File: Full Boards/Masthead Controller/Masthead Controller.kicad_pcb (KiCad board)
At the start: 4 copper layers, 80 x 150.1 mm, 177 parts, among them Q1 2N7002, Q2 2N7002, Q3 BSS138P,215, Q4 BSS138P,215, SW1 SW_MEC_5G, SW2 SW_MEC_5G

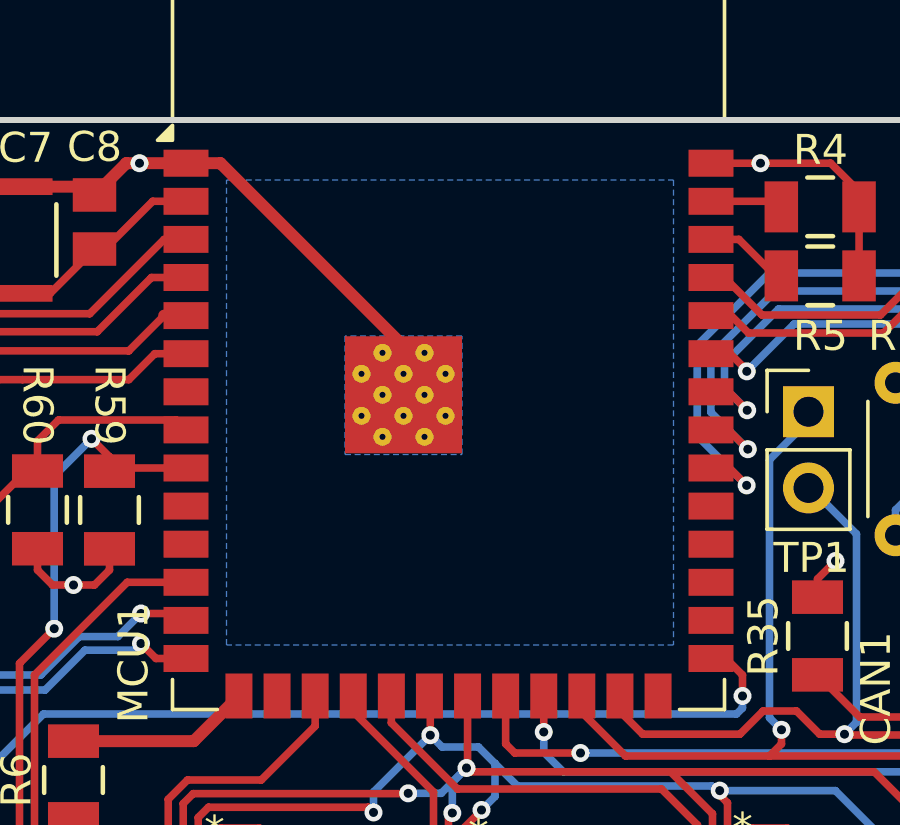
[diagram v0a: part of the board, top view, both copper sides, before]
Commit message: Clones the ESP32-S3-WROOM-1 footprint to bump the vias to 0.3mm. Added a stitched ground under the ESP32 MCU to help further with cooling.
Signed-off-by: digimer <digital.mermaid@gmail.com>
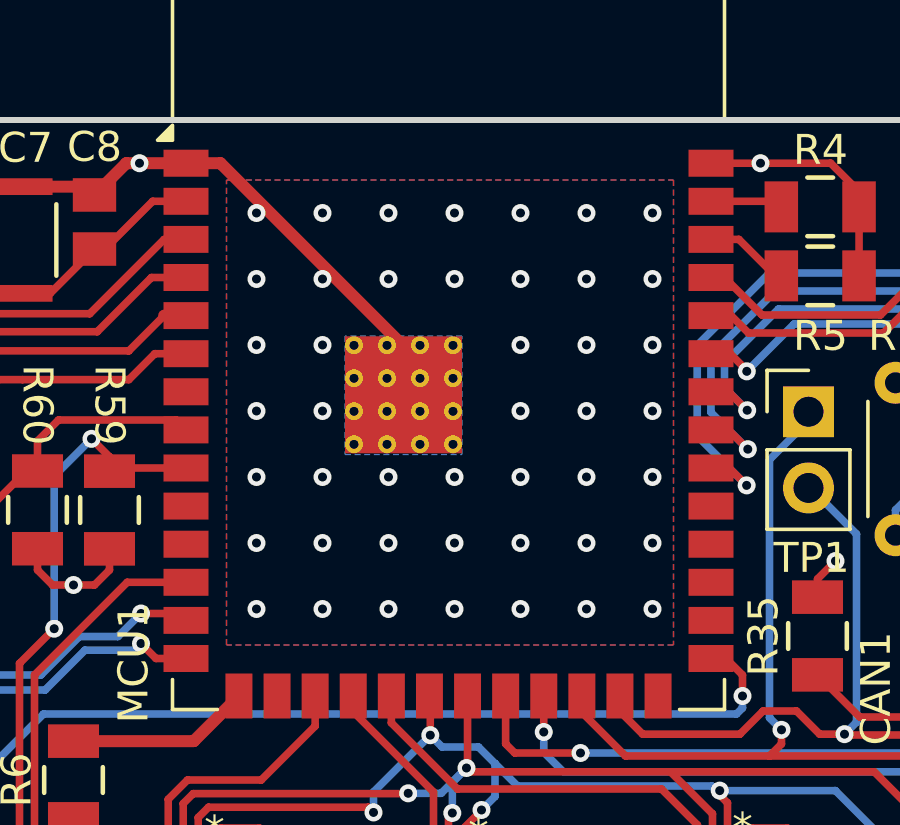
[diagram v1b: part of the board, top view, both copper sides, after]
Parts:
- MCU1: footprint RF_Module:ESP32-S3-WROOM-1 -> mr-stuff:ESP32-S3-WROOM-1
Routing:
- net GND: vias 139 -> 184

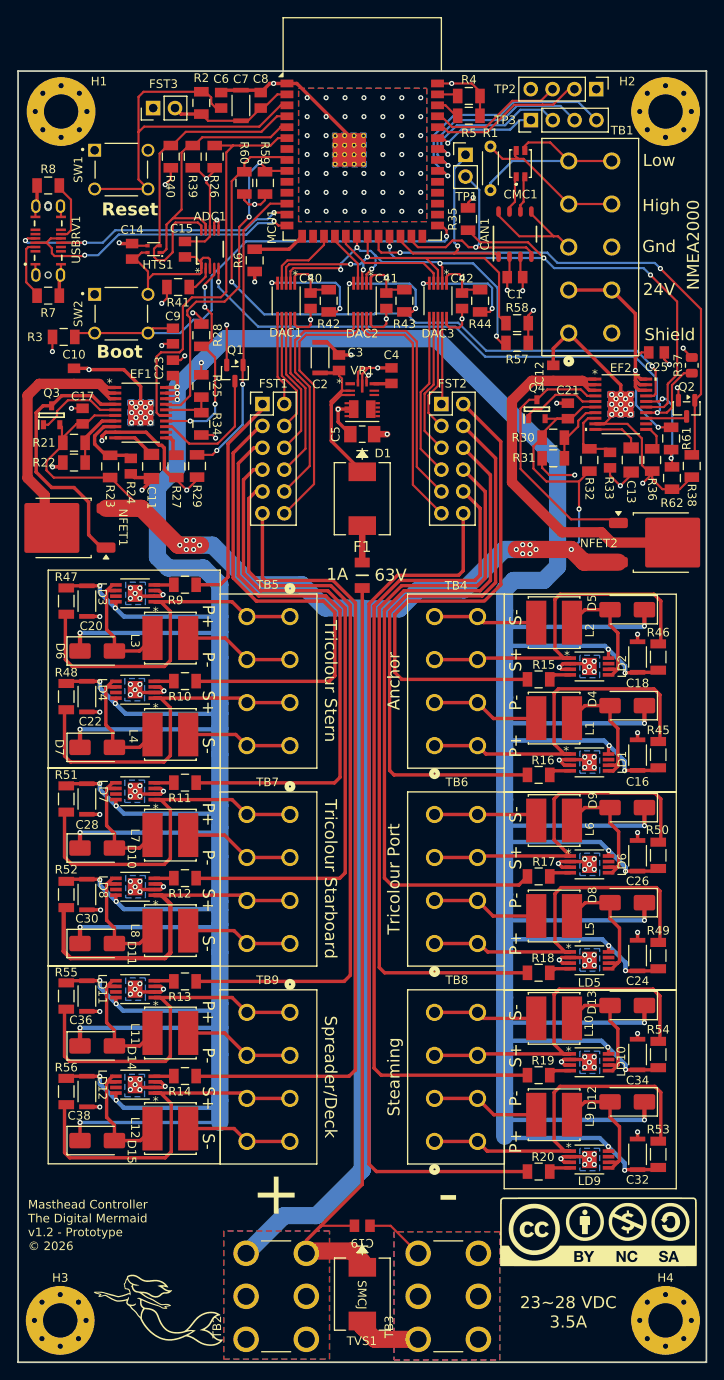
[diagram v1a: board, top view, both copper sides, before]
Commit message: Updated the resistor metadata. This resulted in a bunch of capacitor pins inverting.
Signed-off-by: digimer <digital.mermaid@gmail.com>
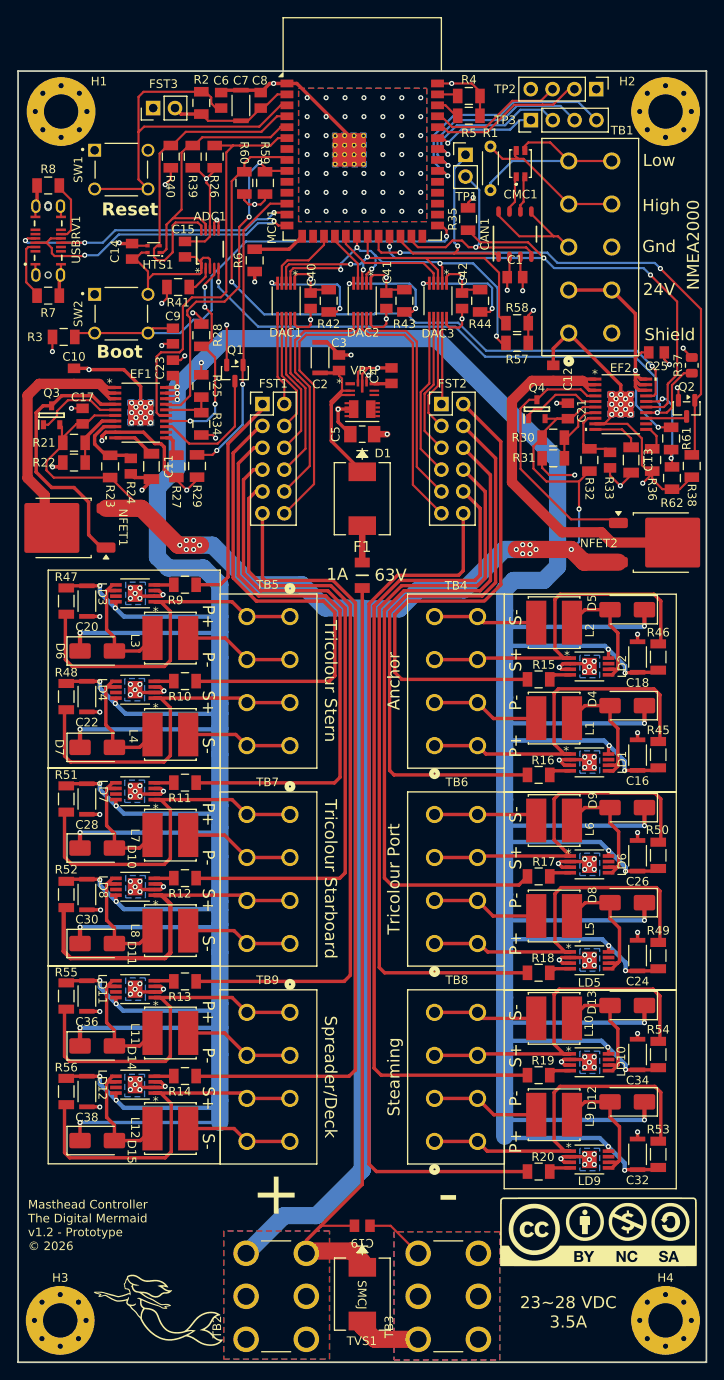
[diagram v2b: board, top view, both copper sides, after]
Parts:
- C1, C10, C12, C15, C17, C21, C23, C25, C3, C40, C41, C42, C8: value 0.1μF -> 0.1uF; footprint mr-stuff:Kyocera AVX 08051A0R8CAT2A -> mr-stuff:Kyocera AVX 0805
- C11, C13: value 0.01μF -> 0.01uF; footprint mr-stuff:Kemet CAPC340180_88N_KEM -> mr-stuff:Kyocera AVX 1206
- C14: value 0.1μF -> 1uF; footprint mr-stuff:Kyocera AVX 08051A0R8CAT2A -> mr-stuff:Kyocera AVX 0805
- C16, C18, C2, C20, C22, C24, C26, C28, C30, C32, C34, C36, C38, C7: value 10μF -> 10uF
- C19: value 1μF -> 1uF
- C4, C6, C9: value 1μF -> 1uF; footprint mr-stuff:Kyocera AVX 08051A0R8CAT2A -> mr-stuff:Kyocera AVX 0805
- C5: value 22μF -> 22uF
- turned C10 to 90 degrees
- turned C12 to 90 degrees
- turned C15 to -90 degrees
- turned C16 to 90 degrees
- turned C17 to 90 degrees
- turned C18 to 90 degrees
- turned C20 to -90 degrees
- turned C21 to 90 degrees
- turned C22 to -90 degrees
- turned C23 to 90 degrees
- turned C24 to 90 degrees
- turned C25 to 0 degrees
- turned C26 to 90 degrees
- turned C28 to -90 degrees
- turned C3 to -90 degrees
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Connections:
- C10 pad 1: GND -> Net-(NFET1-D)
- C10 pad 2: Net-(NFET1-D) -> GND
- C12 pad 1: GND -> Net-(NFET2-D)
- C12 pad 2: Net-(NFET2-D) -> GND
- C15 pad 1: GND -> +3.3V
- C15 pad 2: +3.3V -> GND
- C16 pad 1: GND -> +24V_LED
- C16 pad 2: +24V_LED -> GND
- C17 pad 1: GND -> +24V_ISO
- C17 pad 2: +24V_ISO -> GND
- C18 pad 1: GND -> +24V_LED
- C18 pad 2: +24V_LED -> GND
- C20 pad 1: GND -> +24V_LED
- C20 pad 2: +24V_LED -> GND
- C21 pad 1: GND -> +24V_ISO
- C21 pad 2: +24V_ISO -> GND
- C22 pad 1: GND -> +24V_LED
- C22 pad 2: +24V_LED -> GND
- C23 pad 1: GND -> +24V_LED
- C23 pad 2: +24V_LED -> GND
- C24 pad 1: GND -> +24V_LED
- C24 pad 2: +24V_LED -> GND
- C25 pad 1: GND -> +24V_N2K
- C25 pad 2: +24V_N2K -> GND
- C26 pad 1: GND -> +24V_LED
- C26 pad 2: +24V_LED -> GND
- C28 pad 1: GND -> +24V_LED
- C28 pad 2: +24V_LED -> GND
- C3 pad 1: Net-(VR1-EN) -> GND
- C3 pad 2: GND -> Net-(VR1-EN)
- C30 pad 1: GND -> +24V_LED
- C30 pad 2: +24V_LED -> GND
- C32 pad 1: GND -> +24V_LED
- C32 pad 2: +24V_LED -> GND
- C34 pad 1: GND -> +24V_LED
- C34 pad 2: +24V_LED -> GND
- C36 pad 1: GND -> +24V_LED
- C36 pad 2: +24V_LED -> GND
- C38 pad 1: GND -> +24V_LED
- C38 pad 2: +24V_LED -> GND
- C40 pad 1: +3.3V -> GND
- C40 pad 2: GND -> +3.3V
- C41 pad 1: +3.3V -> GND
- C41 pad 2: GND -> +3.3V
- C42 pad 1: +3.3V -> GND
- C42 pad 2: GND -> +3.3V
- C7 pad 1: Net-(FST3-Pin_2) -> GND
- C7 pad 2: GND -> Net-(FST3-Pin_2)
- C8 pad 1: GND -> Net-(FST3-Pin_2)
- C8 pad 2: Net-(FST3-Pin_2) -> GND
- C9 pad 1: GND -> Net-(MCU1-IO0)
- C9 pad 2: Net-(MCU1-IO0) -> GND

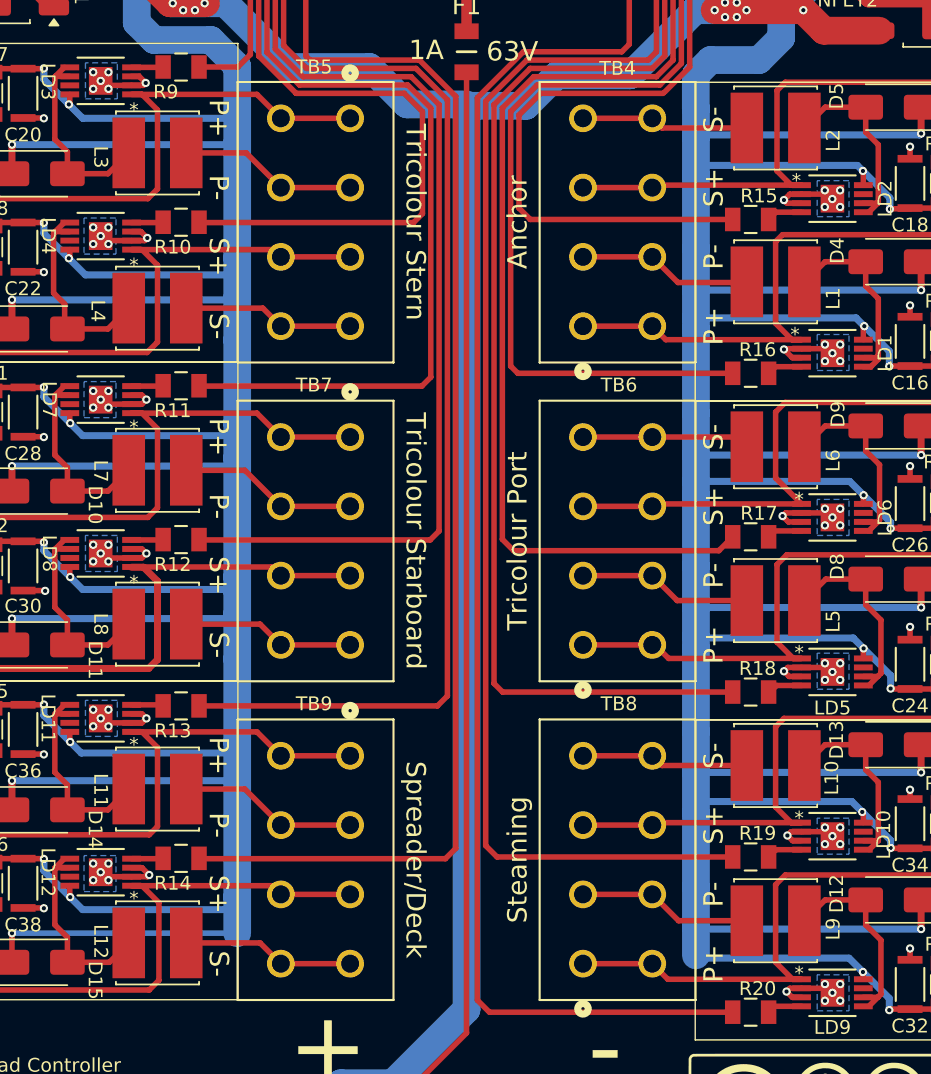
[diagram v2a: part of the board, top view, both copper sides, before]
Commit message: Updated inductors to be better suited per-circuit.
Signed-off-by: digimer <digital.mermaid@gmail.com>
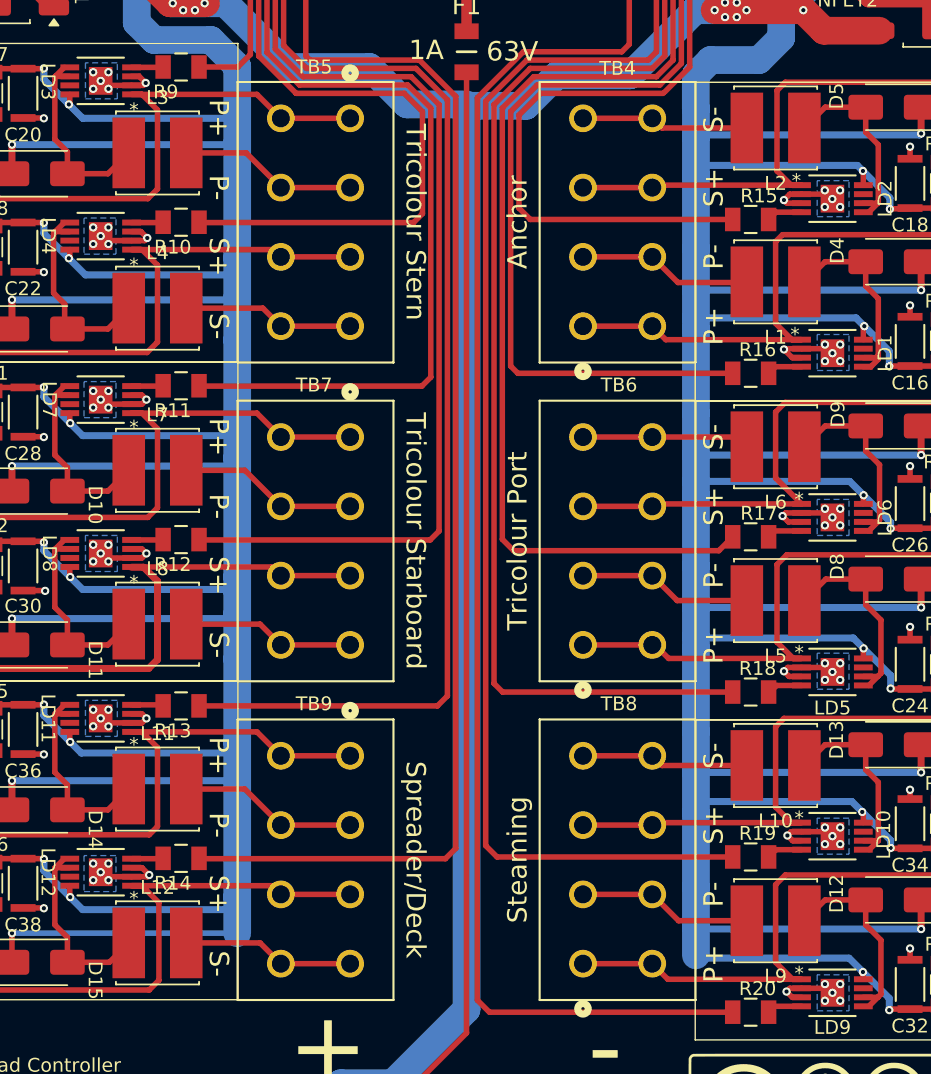
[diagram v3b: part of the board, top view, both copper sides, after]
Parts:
- L1, L2: value SRN6045TA-680M -> 100 uH; footprint mr-stuff:Bourns SRN6045TA-680M -> mr-stuff:Bourns SRN6045TA
- L10, L3, L4, L9: value SRN6045TA-680M -> 220 uH; footprint mr-stuff:Bourns SRN6045TA-680M -> mr-stuff:Bourns SRN6045TA
- L11, L12: value SRN6045TA-680M -> 68 uH; footprint mr-stuff:Bourns SRN6045TA-680M -> mr-stuff:Bourns SRN6045TA
- L5, L6: value SRN6045TA-680M -> 330 uH; footprint mr-stuff:Bourns SRN6045TA-680M -> mr-stuff:Bourns SRN6045TA
- L7, L8: value SRN6045TA-680M -> 470 uH; footprint mr-stuff:Bourns SRN6045TA-680M -> mr-stuff:Bourns SRN6045TA

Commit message: Added a voltage divider reference to ADC1.Pin6 (AIN2) to provide a reference to the +24V_ISO to allow differentiating between input sag and e-fuse fault.
Signed-off-by: digimer <digital.mermaid@gmail.com>
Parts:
- added C27: 0.1uF, mr-stuff:Kyocera AVX 0805, F.Cu at (72.8, 54.5)
- added R63: 100kR, mr-stuff:Stackpole_RNCP1206, F.Cu at (77.3, 54.1)
- added R64: 10kR, mr-stuff:Stackpole_RNCP1206, F.Cu at (75.0, 54.1)
- moved HTS1 4.89 mm to (76.7, 49.2)
- moved C14 3.46 mm to (73.5, 50.8), turned to 180 degrees
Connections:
- ADC1 pad 6: GND -> Net-(ADC1-AIN2)
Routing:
- net +24V_ISO: track 303.9 -> 335.5 mm, vias 14 -> 16
- net Net-(ADC1-AIN2): track 0.00 -> 27.4 mm
- net /I2C_SCL: track 38.6 -> 29.6 mm
- net +3.3V: track 62.5 -> 68.5 mm
- net /I2C_SDA: track 31.2 -> 25.8 mm
- net GND: track 285.8 -> 289.5 mm, vias 184 -> 186
- net /EFUSE_N2K_IMON: track 70.5 -> 71.9 mm
- net /PGOOD_LED: track 39.9 -> 40.8 mm
- net /EFUSE_LED_IMON: track 25.3 -> 26.1 mm
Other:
- board text added: "25~28 VDC 3.5A"
- board text removed: "23~28 VDC 3.5A"

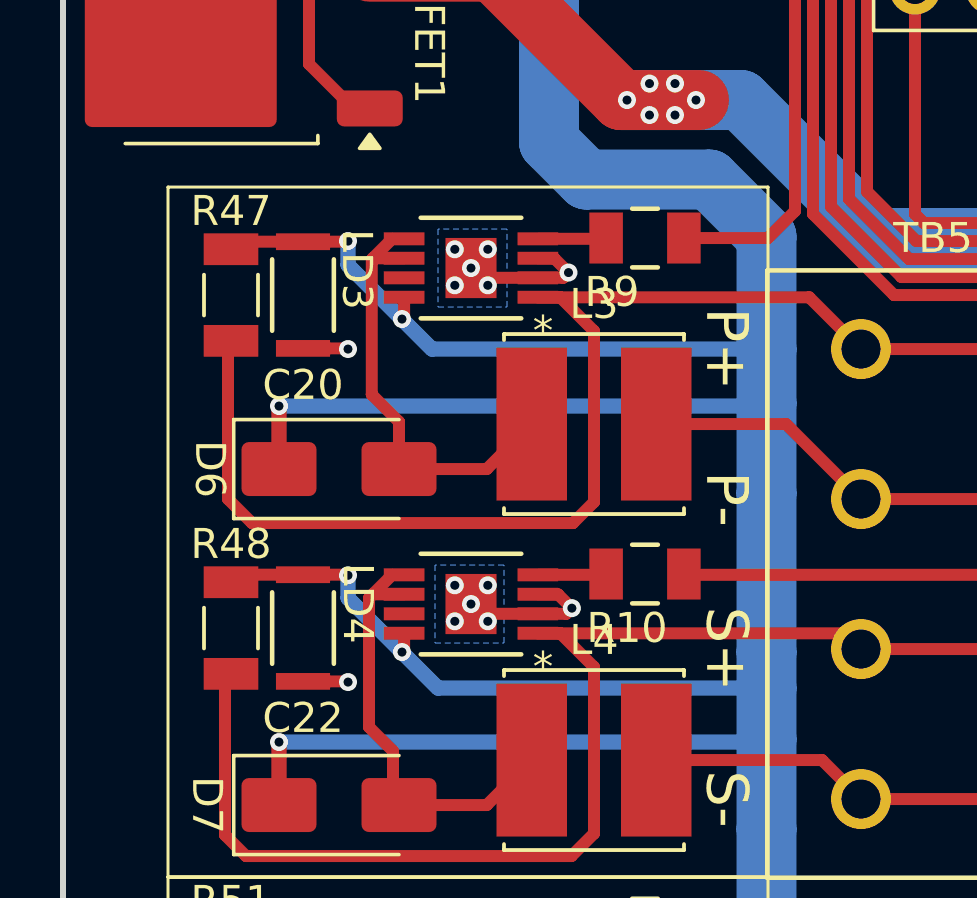
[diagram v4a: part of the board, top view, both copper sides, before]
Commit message: Test refactor of the LD3 to D6 placement to reduce the loop length and hopefully reduce the ringing in VHF bands.
Signed-off-by: digimer <digital.mermaid@gmail.com>
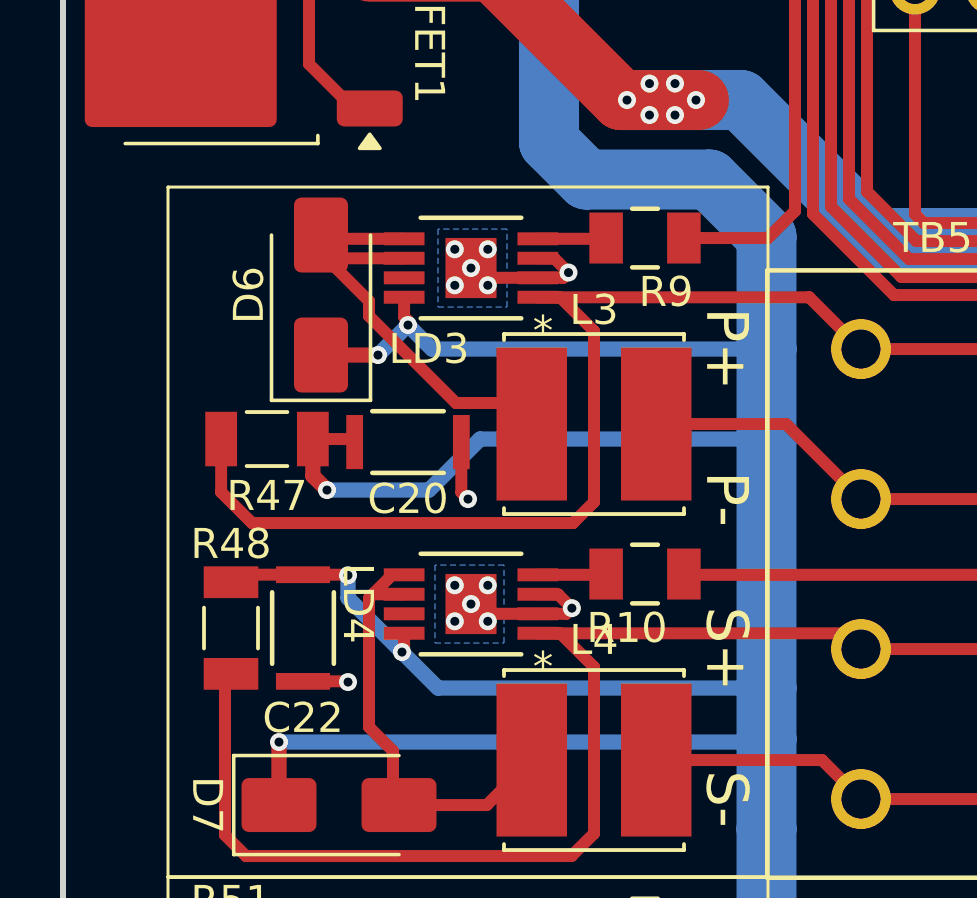
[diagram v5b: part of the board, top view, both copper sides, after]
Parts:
- moved C20 6.02 mm to (71.5, 99.8), turned to 0 degrees
- moved D6 5.83 mm to (68.6, 94.9), turned to 90 degrees
- moved R47 4.95 mm to (66.8, 99.7), turned to 180 degrees
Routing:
- net +24V_LED: track 700.9 -> 697.4 mm
- net Net-(LD3-ISENSE): track 42.5 -> 39.4 mm
- net Net-(D6-A): track 14.4 -> 16.2 mm
